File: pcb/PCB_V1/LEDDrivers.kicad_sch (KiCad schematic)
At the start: 52 parts, among them J711 LED +/- (return isolated), J721 LED +/- (return isolated), J731 LED +/- (return isolated), Q711 CSD19534Q5A, Q721 CSD19538Q3A, U700 SN74LVC1G08DBVR, U710 AL8853S-13, U720 AL8853S-13

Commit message: pcb: integrate reviewed parts and validate initial 100mm placement
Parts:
- J711, J721, J731: footprint TerminalBlock_Phoenix:TerminalBlock_Phoenix_MKDS-1,5-2-5.08_1x02_P5.08mm_Horizontal -> GrowBox:TerminalBlock_KANGNEX_WJ500V-5.08_1x02_P5.08mm_Horizontal
- R715: LCSC (none) -> C19633795; MPN (none) -> LR123WF270MT4E; Manufacturer (none) -> UNI-ROYAL
- R716: value 0.182 1% >=1W -> 0.18 1% 2W 50ppm; LCSC (none) -> C48533605; MPN (none) -> FRM252WFR180TM; Manufacturer (none) -> FOJAN
- R725: LCSC (none) -> C52015951; MPN (none) -> HIXD25NR047F; Manufacturer (none) -> RVR
- R726: LCSC (none) -> C22464907; MPN (none) -> RLH12FTCR430; Manufacturer (none) -> TA-I
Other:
- note added: "0.17 DRAFT: power input 24 V; AL8853 bias 12 V. CH1 back to SRP1770TA-470M / 0.027 ohm (OCP headroom). CH1 1.111 A; CH2 0.465 A total. Qualification pending."
- note added: "CH1: 1.111 A nominal / panel"
- note added: "DRAFT: 120 kHz; OVP nominal 65.2 V. 100 V output parts. Current calculations: DESIGN.md / LED_power_v17.txt."
- note removed: "0.16 DRAFT: power input 24 V; AL8853 bias 12 V. CH1 back to SRP1770TA-470M / 0.027 ohm (OCP headroom). CH1 1.099 A; CH2 0.465 A total. Qualification pending."
- note removed: "CH1: 1.099 A nominal / panel"
- note removed: "DRAFT: 120 kHz; OVP nominal 65.2 V. 100 V output parts. Current calculations: REDESIGN_24V.md / LED_power_v15.txt."
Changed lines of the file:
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@@
 	(title_block
 		(title "07 - AL8853 LED drivers, 24 V input, 2 channels")
-		(date "2026-09-27")
-		(rev "0.16-DRAFT")
+		(date "2026-09-28")
+		(rev "0.17-DRAFT")
 		(company "GrowBox controller")
 		(comment 1 "Engineering draft; startup, thermal and fault qualification pending")
@@
 		)
 	)
-	(text "DRAFT: 120 kHz; OVP nominal 65.2 V. 100 V output parts. Current calculations: REDESIGN_24V.md / LED_power_v15.txt."
+	(text "DRAFT: 120 kHz; OVP nominal 65.2 V. 100 V output parts. Current calculations: DESIGN.md / LED_power_v17.txt."
 		(exclude_from_sim no)
 		(at 20.32 378.46 0)
@@
 		)
 	)
-	(text "CH1: 1.099 A nominal / panel"
+	(text "CH1: 1.111 A nominal / panel"
 		(exclude_from_sim no)
 		(at 20.32 80.01 0)
@@
 		)
 	)
-	(text "0.16 DRAFT: power input 24 V; AL8853 bias 12 V. CH1 back to SRP1770TA-470M / 0.027 ohm (OCP headroom). CH1 1.099 A; CH2 0.465 A total. Qualification pending."
+	(text "0.17 DRAFT: power input 24 V; AL8853 bias 12 V. CH1 back to SRP1770TA-470M / 0.027 ohm (OCP headroom). CH1 1.111 A; CH2 0.465 A total. Qualification pending."
 		(exclude_from_sim no)
 		(at 20.32 22.86 0)
@@
 			)
 		)
-		(property "Datasheet" ""
+		(property "Datasheet" "https://datasheet.lcsc.com/datasheet/pdf/1e1d842ae9bed7ba5f7b9bc74b663d5b.pdf"
 			(at 250.19 156.21 0)
 			(hide yes)
@@
 			)
 		)
+		(property "Manufacturer" "UNI-ROYAL"
+			(at 250.19 156.21 0)
+			(hide yes)
+			(show_name no)
+			(do_not_autoplace no)
+			(effects
+				(font
+					(size 1 1)
+				)
+				(justify left)
+			)
+		)
+		(property "MPN" "LR123WF270MT4E"
+			(at 250.19 156.21 0)
+			(hide yes)
+			(show_name no)
+			(do_not_autoplace no)
+			(effects
+				(font
+					(size 1 1)
+				)
+				(justify left)
+			)
+		)
+		(property "LCSC" "C19633795"
+			(at 250.19 156.21 0)
+			(hide yes)
+			(show_name no)
+			(do_not_autoplace no)
+			(effects
+				(font
+					(size 1 1)
+				)
+				(justify left)
+			)
+		)
 	)
 	(symbol
@@
 			)
 		)
-		(property "Datasheet" ""
+		(property "Datasheet" "https://datasheet.lcsc.com/datasheet/pdf/fb9056c7c2bdf119444a6a2c20d137ad.pdf"
 			(at 444.5 223.52 0)
 			(hide yes)
@@
 			)
 		)
+		(property "Manufacturer" "TA-I"
+			(at 444.5 223.52 0)
+			(hide yes)
+			(show_name no)
+			(do_not_autoplace no)
+			(effects
+				(font
+					(size 1 1)
+				)
+				(justify left)
+			)
+		)
+		(property "MPN" "RLH12FTCR430"
+			(at 444.5 223.52 0)
+			(hide yes)
+			(show_name no)
+			(do_not_autoplace no)
+			(effects
+				(font
+					(size 1 1)
+				)
+				(justify left)
+			)
+		)
+		(property "LCSC" "C22464907"
+			(at 444.5 223.52 0)
+			(hide yes)
+			(show_name no)
+			(do_not_autoplace no)
+			(effects
+				(font
+					(size 1 1)
+				)
+				(justify left)
+			)
+		)
 	)
 	(symbol
@@
 			)
 		)
-		(property "Footprint" "TerminalBlock_Phoenix:TerminalBlock_Phoenix_MKDS-1,5-2-5.08_1x02_P5.08mm_Horizontal"
+		(property "Footprint" "GrowBox:TerminalBlock_KANGNEX_WJ500V-5.08_1x02_P5.08mm_Horizontal"
 			(at 449.58 298.45 0)
 			(hide yes)
@@
 			)
 		)
-		(property "Datasheet" "https://www.bourns.com/docs/product-datasheets/srp1265a.pdf"
+		(property "Datasheet" "https://www.bourns.com/docs/Product-Datasheets/SRP1770TA.pdf"
 			(at 165.1 97.79 90)
 			(hide yes)
@@
 			)
 		)
-		(property "Footprint" "TerminalBlock_Phoenix:TerminalBlock_Phoenix_MKDS-1,5-2-5.08_1x02_P5.08mm_Horizontal"
+		(property "Footprint" "GrowBox:TerminalBlock_KANGNEX_WJ500V-5.08_1x02_P5.08mm_Horizontal"
 			(at 449.58 198.12 0)
 			(hide yes)
@@
 			)
 		)
-		(property "Value" "0.182 1% >=1W"
+		(property "Value" "0.18 1% 2W 50ppm"
 			(at 448.31 124.46 0)
 			(show_name no)
@@
 			)
 		)
-		(property "Datasheet" ""
+		(property "Datasheet" "https://datasheet.lcsc.com/datasheet/pdf/b47da348e6587de9f1f028172ba2b8ea.pdf"
 			(at 444.5 123.19 0)
 			(hide yes)
@@
 			)
 		)
+		(property "Manufacturer" "FOJAN"
+			(at 444.5 123.19 0)
+			(hide yes)
+			(show_name no)
+			(do_not_autoplace no)
+			(effects
+				(font
+					(size 1 1)
+				)
+				(justify left)
+			)
+		)
+		(property "MPN" "FRM252WFR180TM"
+			(at 444.5 123.19 0)
+			(hide yes)
+			(show_name no)
+			(do_not_autoplace no)
+			(effects
+				(font
+					(size 1 1)
+				)
+				(justify left)
+			)
+		)
+		(property "LCSC" "C48533605"
+			(at 444.5 123.19 0)
+			(hide yes)
+			(show_name no)
+			(do_not_autoplace no)
+			(effects
+				(font
+					(size 1 1)
+				)
+				(justify left)
+			)
+		)
 	)
 	(symbol
@@
 			)
 		)
-		(property "Footprint" "TerminalBlock_Phoenix:TerminalBlock_Phoenix_MKDS-1,5-2-5.08_1x02_P5.08mm_Horizontal"
+		(property "Footprint" "GrowBox:TerminalBlock_KANGNEX_WJ500V-5.08_1x02_P5.08mm_Horizontal"
 			(at 449.58 97.79 0)
 			(hide yes)
@@
 			)
 		)
-		(property "Datasheet" ""
+		(property "Datasheet" "https://datasheet.lcsc.com/datasheet/pdf/4c5de85c3e790e36d40c067847f05fa3.pdf"
 			(at 250.19 256.54 0)
 			(hide yes)
@@
 			)
 		)
+		(property "Manufacturer" "RVR"
+			(at 250.19 256.54 0)
+			(hide yes)
+			(show_name no)
+			(do_not_autoplace no)
+			(effects
+				(font
+					(size 1 1)
+				)
+				(justify left)
+			)
+		)
+		(property "MPN" "HIXD25NR047F"
+			(at 250.19 256.54 0)
+			(hide yes)
+			(show_name no)
+			(do_not_autoplace no)
+			(effects
+				(font
+					(size 1 1)
+				)
+				(justify left)
+			)
+		)
+		(property "LCSC" "C52015951"
+			(at 250.19 256.54 0)
+			(hide yes)
+			(show_name no)
+			(do_not_autoplace no)
+			(effects
+				(font
+					(size 1 1)
+				)
+				(justify left)
+			)
+		)

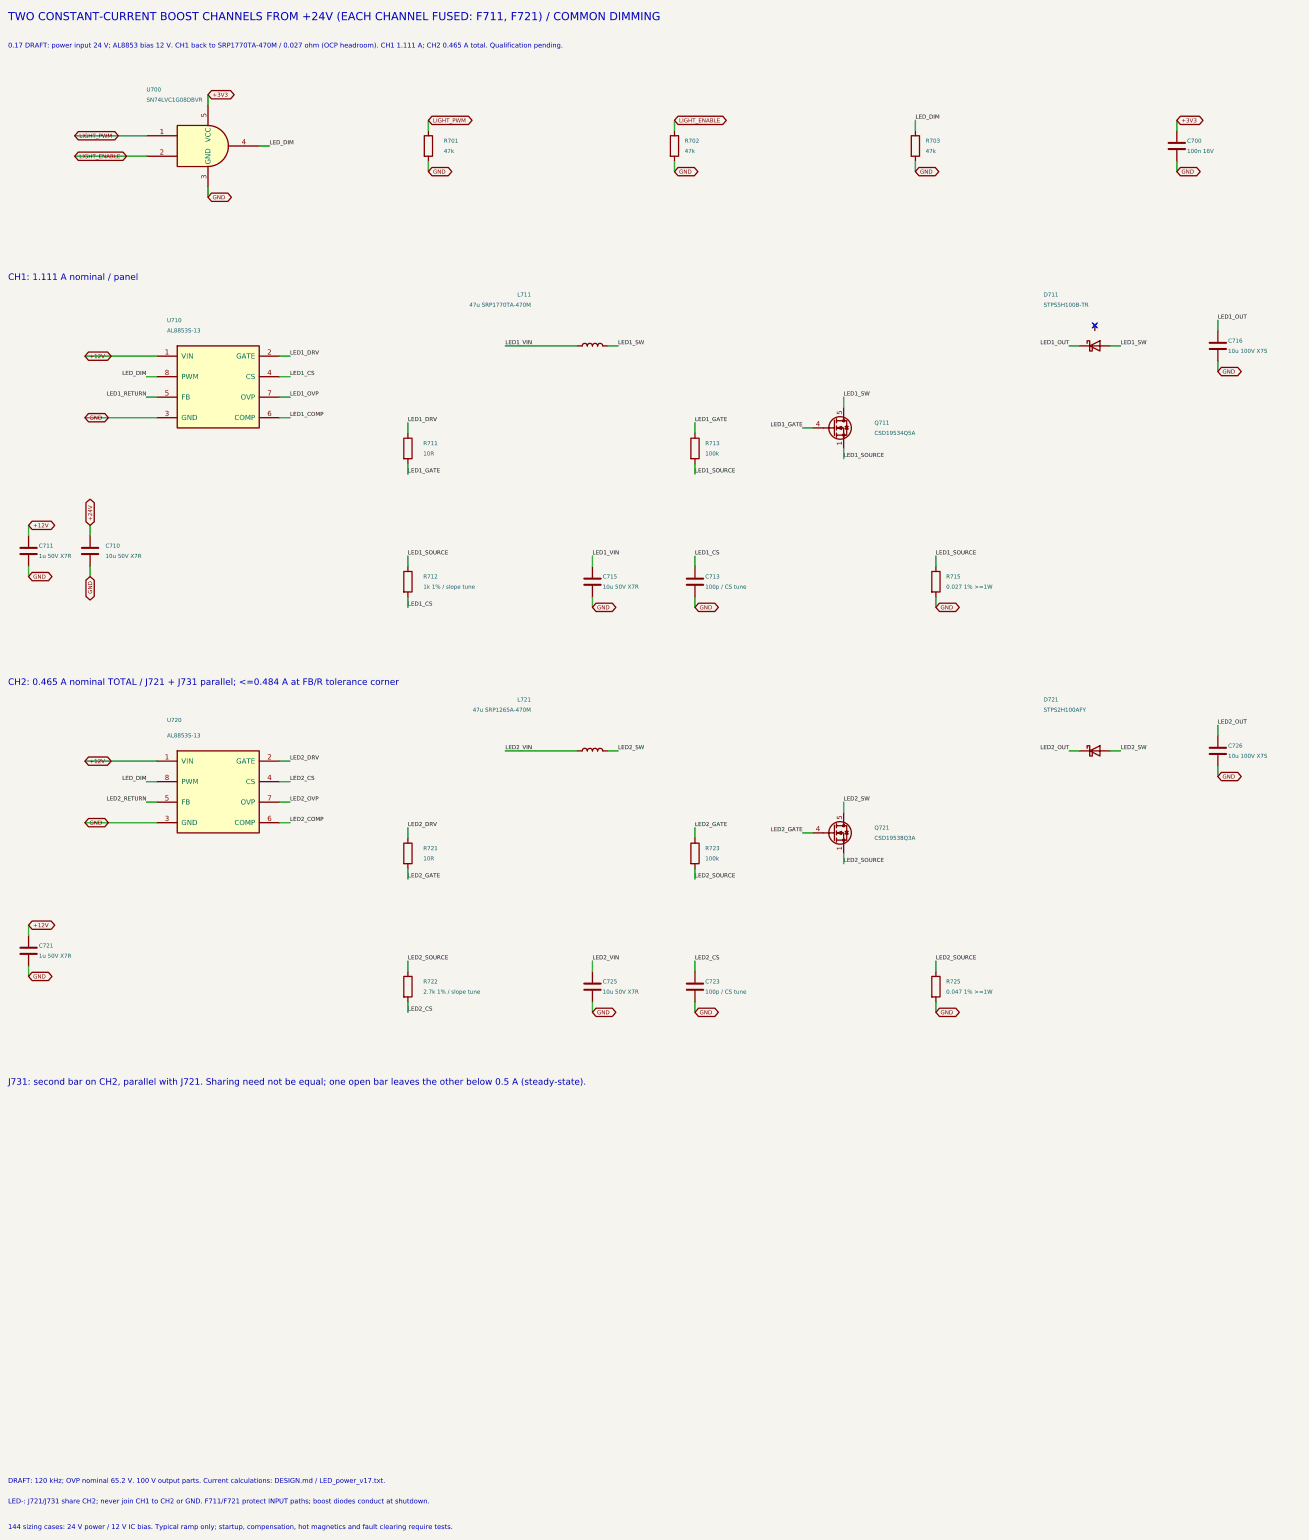
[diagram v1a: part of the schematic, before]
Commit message: pcb: simplify passives and microSD circuitry for revision 0.18
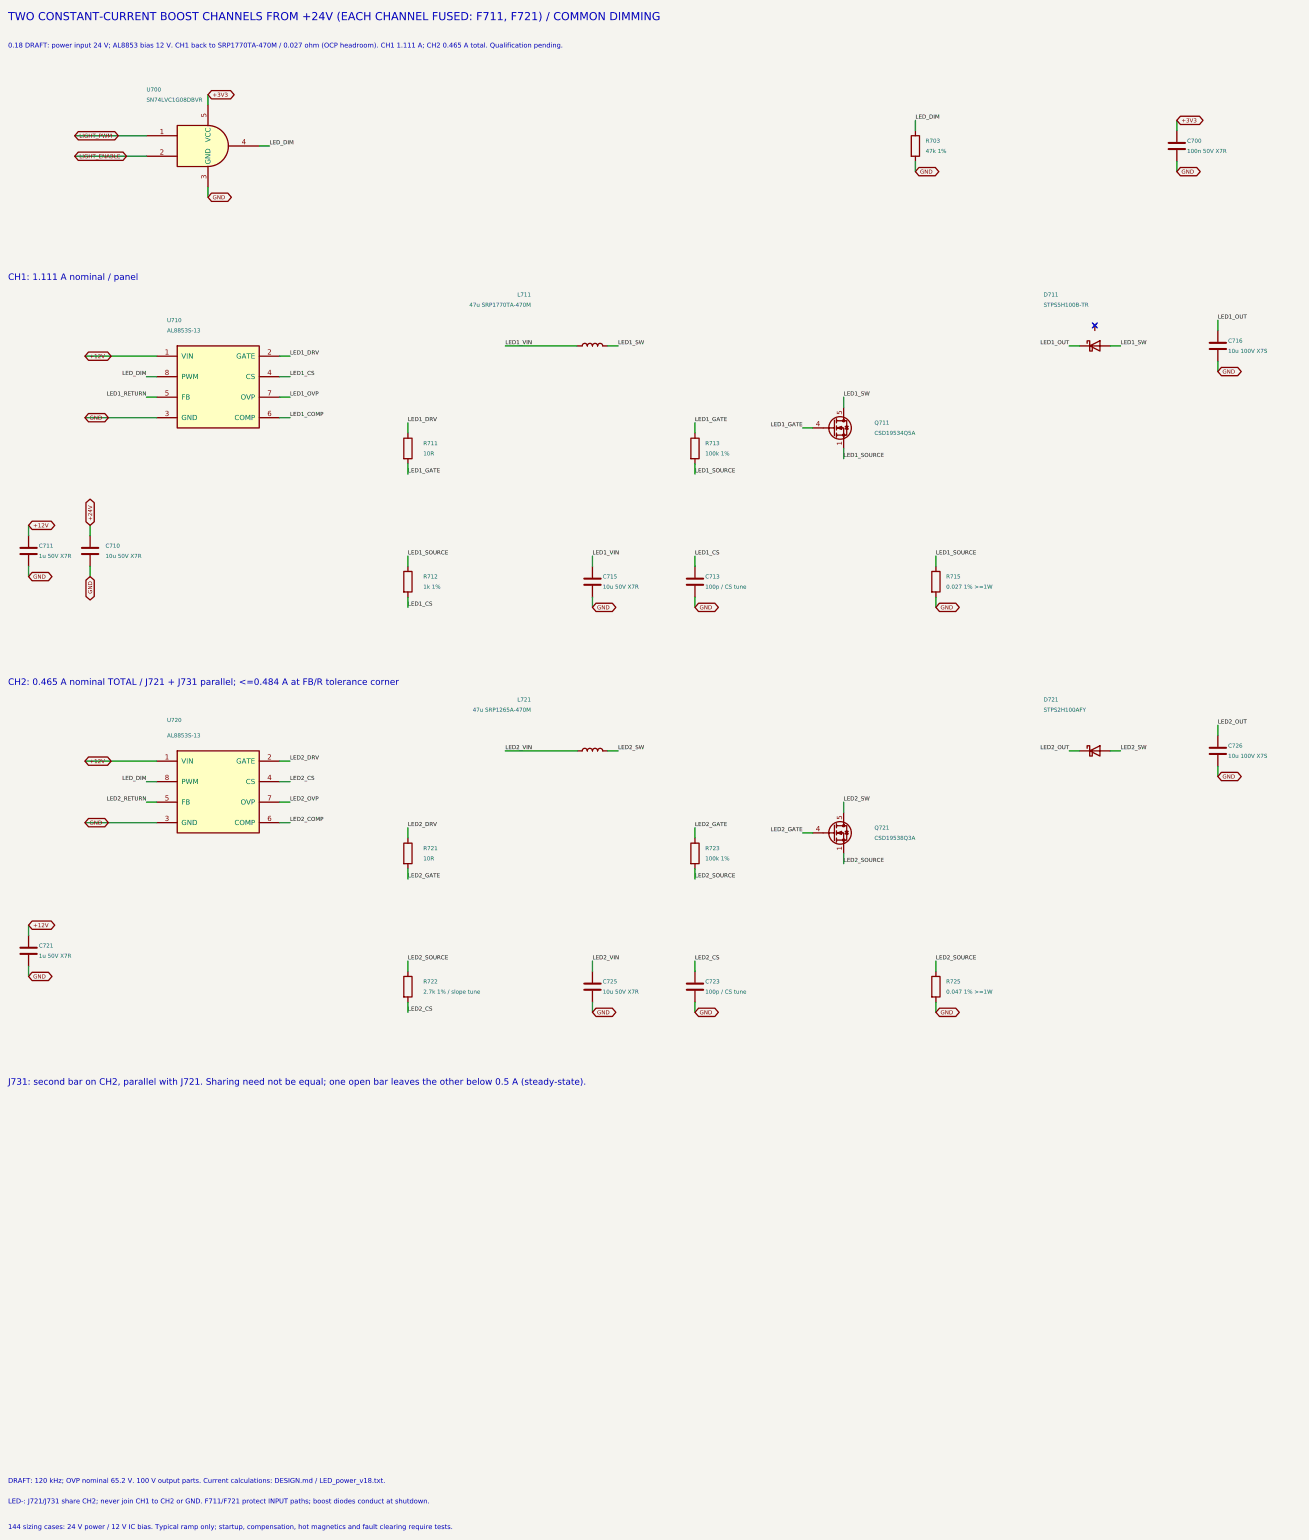
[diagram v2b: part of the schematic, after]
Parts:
- removed R701, R702: 47k, Resistor_SMD:R_0603_1608Metric, symbol Device:R
- C700: value 100n 16V -> 100n 50V X7R; LCSC (none) -> C1591; MPN (none) -> CL10B104KB8NNNC; Manufacturer (none) -> Samsung
- R703: value 47k -> 47k 1%; LCSC (none) -> C105579; MPN (none) -> RC0603FR-0747KL; Manufacturer (none) -> Yageo
- R712: value 1k 1% / slope tune -> 1k 1%; LCSC (none) -> C21190; MPN (none) -> 0603WAF1001T5E; Manufacturer (none) -> UNI-ROYAL
- R713, R723: value 100k -> 100k 1%; LCSC (none) -> C25803; MPN (none) -> 0603WAF1003T5E; Manufacturer (none) -> UNI-ROYAL
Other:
- note added: "0.18 DRAFT: power input 24 V; AL8853 bias 12 V. CH1 back to SRP1770TA-470M / 0.027 ohm (OCP headroom). CH1 1.111 A; CH2 0.465 A total. Qualification pending."
- note added: "DRAFT: 120 kHz; OVP nominal 65.2 V. 100 V output parts. Current calculations: DESIGN.md / LED_power_v18.txt."
- note removed: "0.17 DRAFT: power input 24 V; AL8853 bias 12 V. CH1 back to SRP1770TA-470M / 0.027 ohm (OCP headroom). CH1 1.111 A; CH2 0.465 A total. Qualification pending."
- note removed: "DRAFT: 120 kHz; OVP nominal 65.2 V. 100 V output parts. Current calculations: DESIGN.md / LED_power_v17.txt."
